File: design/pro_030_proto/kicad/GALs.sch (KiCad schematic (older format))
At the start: 11 parts, among them IC2 ATF22V10C, IC3 ATF22V10C, IC4 ATF22V10C, IC5 ATF22V10C

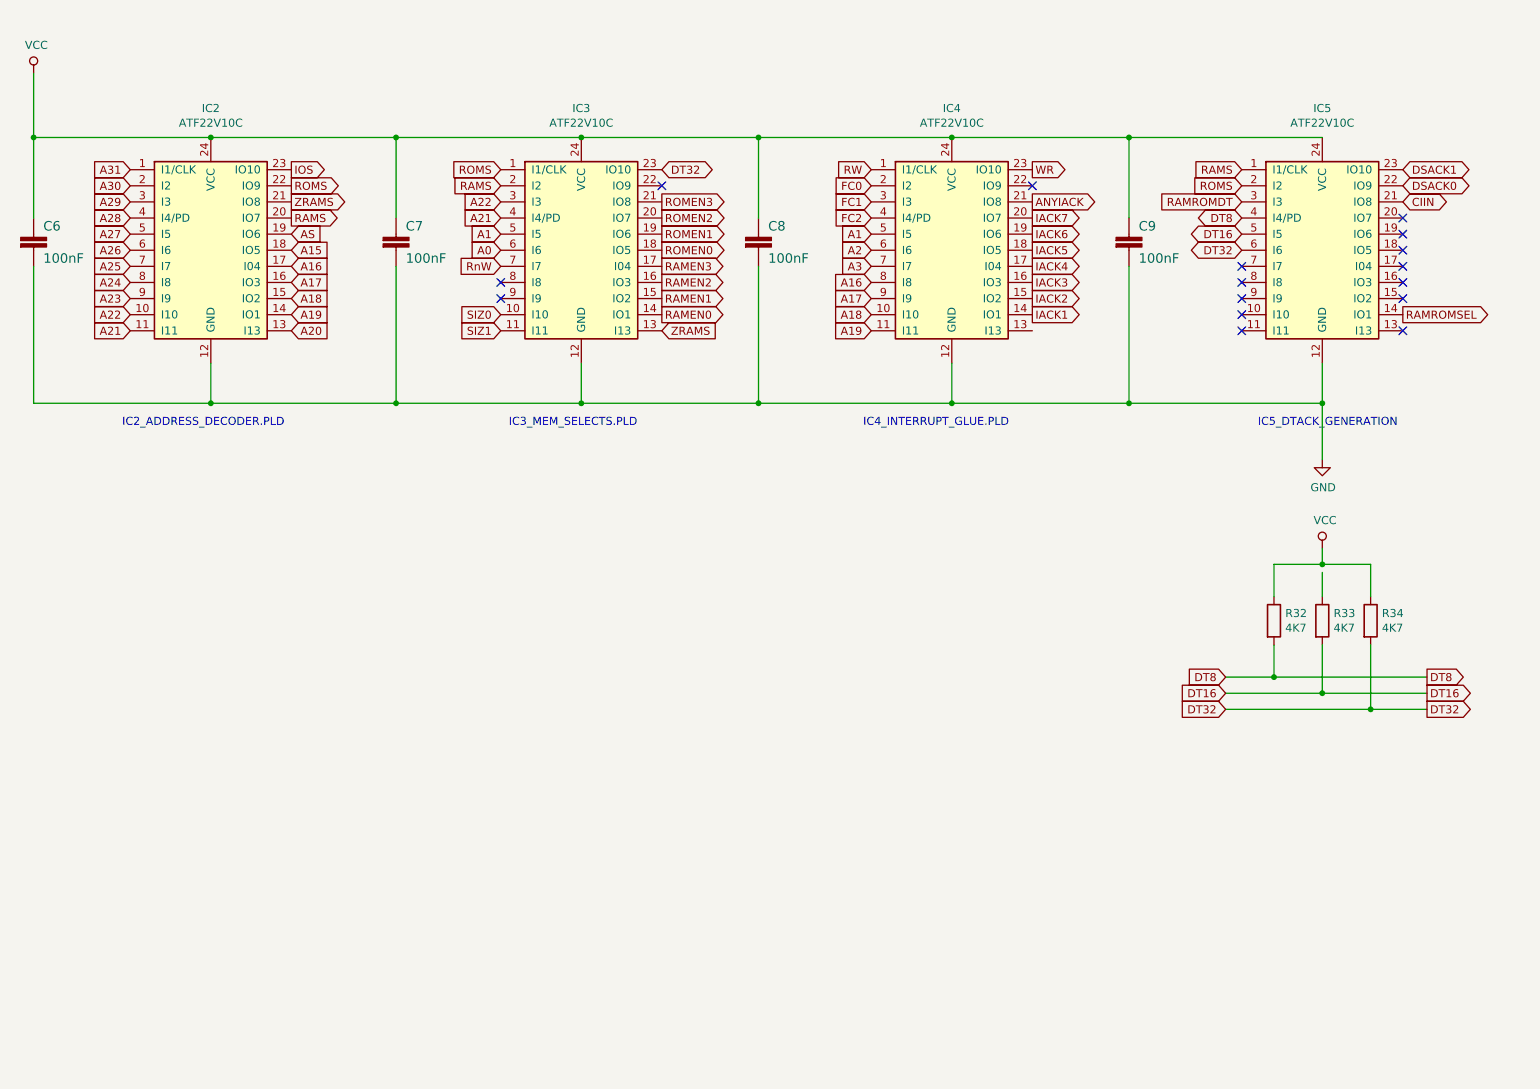
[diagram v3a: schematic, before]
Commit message: Interrupts + Xosera schematic, re-annotate
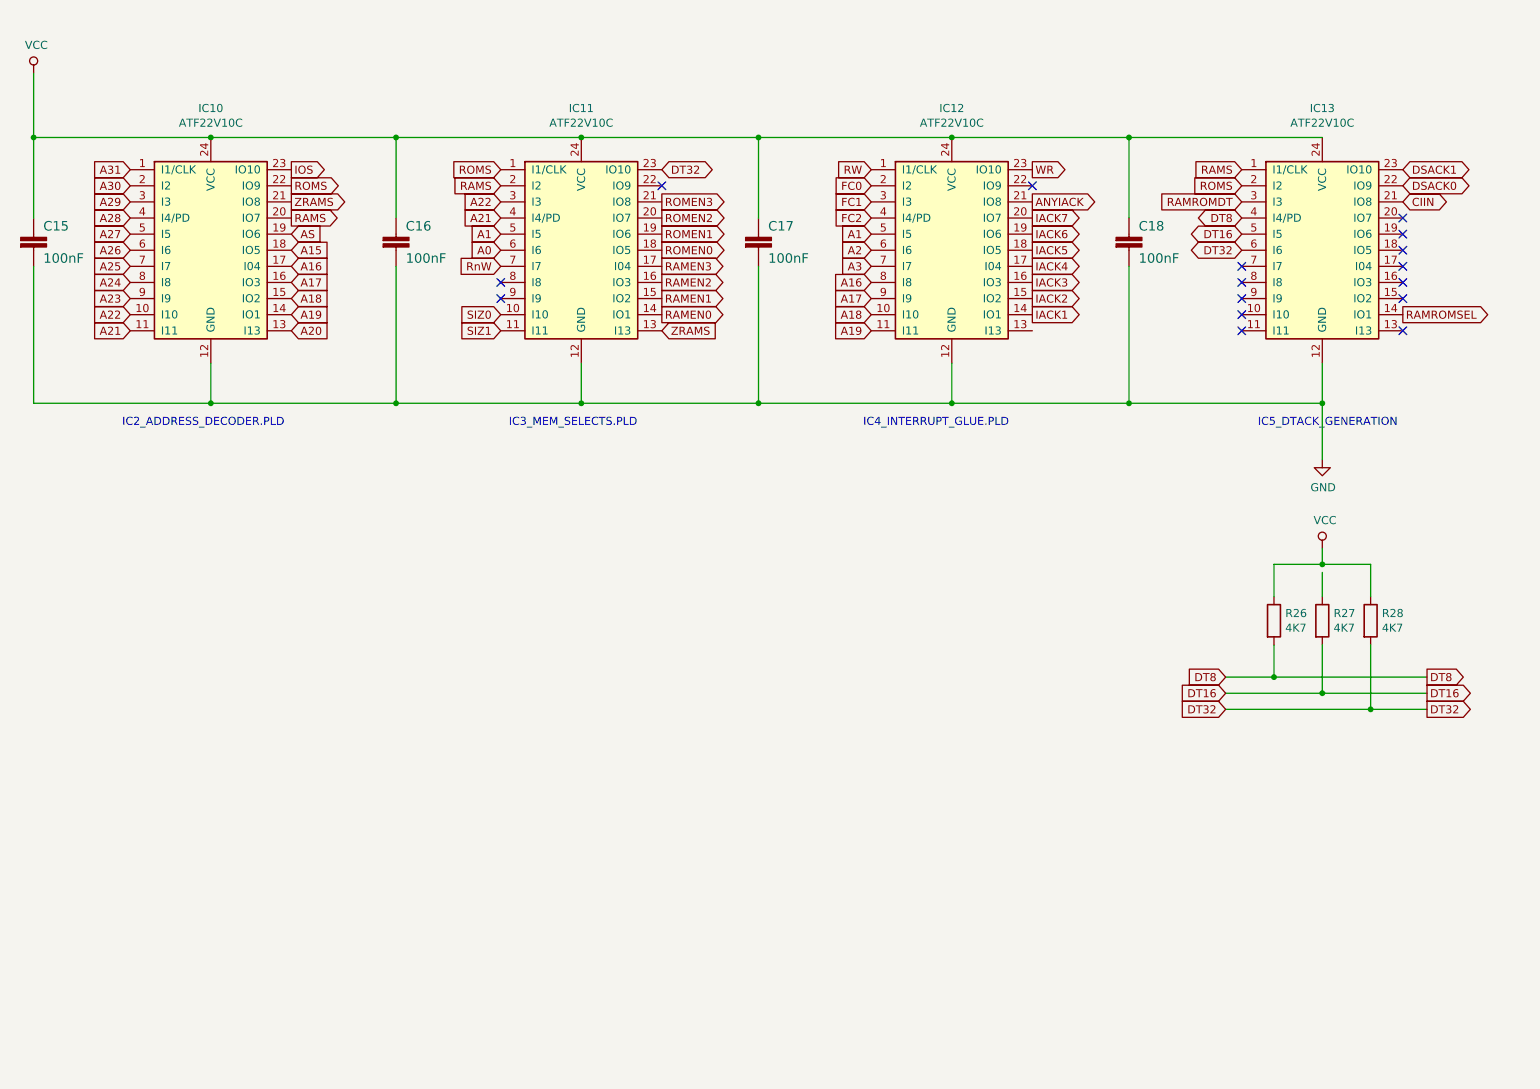
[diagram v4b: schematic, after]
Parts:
- renumbered C6 to C15, C7 to C16, C8 to C17, C9 to C18, IC2 to IC10, IC3 to IC11, IC4 to IC12, IC5 to IC13, R32 to R26, R33 to R27, R34 to R28
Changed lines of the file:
@@
 $Descr A4 11693 8268
 encoding utf-8
-Sheet 7 10
+Sheet 7 13
 Title "rosco_m68k Pro (030) Prototype"
 Date "2021-07-24"
@@
 AR Path="/5E53B810/60FE89A7" Ref="C?"  Part="1"
 AR Path="/5E53B952/60FE89A7" Ref="C?"  Part="1"
-AR Path="/6103896C/60FE89A7" Ref="C7"  Part="1"
-F 0 "C7" H 3610 2165 59  0000 L BNN
+AR Path="/6103896C/60FE89A7" Ref="C16"  Part="1"
+F 0 "C16" H 3610 2165 59  0000 L BNN
 F 1 "100nF" H 3610 1965 59  0000 L BNN
 F 2 "Capacitor_THT:C_Rect_L4.0mm_W2.5mm_P2.50mm" H 3550 2150 50  0001 C CNN
@@
 AR Path="/5E53B810/60F35442" Ref="C?"  Part="1"
 AR Path="/5E53B952/60F35442" Ref="C?"  Part="1"
-AR Path="/6103896C/60F35442" Ref="C8"  Part="1"
-F 0 "C8" H 5860 2165 59  0000 L BNN
+AR Path="/6103896C/60F35442" Ref="C17"  Part="1"
+F 0 "C17" H 5860 2165 59  0000 L BNN
 F 1 "100nF" H 5860 1965 59  0000 L BNN
 F 2 "Capacitor_THT:C_Rect_L4.0mm_W2.5mm_P2.50mm" H 5800 2150 50  0001 C CNN
@@
 AR Path="/5E53B810/60F343B0" Ref="C?"  Part="1"
 AR Path="/5E53B952/60F343B0" Ref="C?"  Part="1"
-AR Path="/6103896C/60F343B0" Ref="C6"  Part="1"
-F 0 "C6" H 1360 2165 59  0000 L BNN
+AR Path="/6103896C/60F343B0" Ref="C15"  Part="1"
+F 0 "C15" H 1360 2165 59  0000 L BNN
 F 1 "100nF" H 1360 1965 59  0000 L BNN
 F 2 "Capacitor_THT:C_Rect_L4.0mm_W2.5mm_P2.50mm" H 1300 2150 50  0001 C CNN
@@
 	4700 2950 4700 3200
 $Comp
-L power:GND #PWR0124
+L power:GND #PWR031
 U 1 1 60F311F4
 P 9300 3550
-F 0 "#PWR0124" H 9300 3300 50  0001 C CNN
+F 0 "#PWR031" H 9300 3300 50  0001 C CNN
 F 1 "GND" H 9305 3377 50  0000 C CNN
 F 2 "" H 9300 3550 50  0001 C CNN
@@
 $EndComp
 $Comp
-L power:VCC #PWR0125
+L power:VCC #PWR030
 U 1 1 60F30787
 P 1300 1150
-F 0 "#PWR0125" H 1300 1000 50  0001 C CNN
+F 0 "#PWR030" H 1300 1000 50  0001 C CNN
 F 1 "VCC" H 1317 1323 50  0000 C CNN
 F 2 "" H 1300 1150 50  0001 C CNN
@@
 ROMS
 $Comp
-L rosco_m68k:GAL22V10 IC3
+L rosco_m68k:GAL22V10 IC11
 U 1 1 60F2CECC
 P 4700 2250
-F 0 "IC3" H 4700 3131 50  0000 C CNN
+F 0 "IC11" H 4700 3131 50  0000 C CNN
 F 1 "ATF22V10C" H 4700 3040 50  0000 C CNN
 F 2 "Package_DIP:DIP-24_W7.62mm_Socket_LongPads" H 4700 2250 50  0001 C CNN
@@
 A31
 $Comp
-L rosco_m68k:GAL22V10 IC2
+L rosco_m68k:GAL22V10 IC10
 U 1 1 60F1E34A
 P 2400 2250
-F 0 "IC2" H 2400 3131 50  0000 C CNN
+F 0 "IC10" H 2400 3131 50  0000 C CNN
 F 1 "ATF22V10C" H 2400 3040 50  0000 C CNN
 F 2 "Package_DIP:DIP-24_W7.62mm_Socket_LongPads" H 2400 2250 50  0001 C CNN
@@
 	7000 3200 7000 2950
 $Comp
-L rosco_m68k:GAL22V10 IC4
+L rosco_m68k:GAL22V10 IC12
 U 1 1 60FE4F51
 P 7000 2250
-F 0 "IC4" H 7000 3131 50  0000 C CNN
+F 0 "IC12" H 7000 3131 50  0000 C CNN
 F 1 "ATF22V10C" H 7000 3040 50  0000 C CNN
 F 2 "Package_DIP:DIP-24_W7.62mm_Socket_LongPads" H 7000 2250 50  0001 C CNN
@@
 AR Path="/5E53B810/610AB2E1" Ref="C?"  Part="1"
 AR Path="/5E53B952/610AB2E1" Ref="C?"  Part="1"
-AR Path="/6103896C/610AB2E1" Ref="C9"  Part="1"
-F 0 "C9" H 8160 2165 59  0000 L BNN
+AR Path="/6103896C/610AB2E1" Ref="C18"  Part="1"
+F 0 "C18" H 8160 2165 59  0000 L BNN
 F 1 "100nF" H 8160 1965 59  0000 L BNN
 F 2 "Capacitor_THT:C_Rect_L4.0mm_W2.5mm_P2.50mm" H 8100 2150 50  0001 C CNN
@@
 NoConn ~ 7500 1850
 $Comp
-L rosco_m68k:GAL22V10 IC5
+L rosco_m68k:GAL22V10 IC13
 U 1 1 610AB2F4
 P 9300 2250
-F 0 "IC5" H 9300 3131 50  0000 C CNN
+F 0 "IC13" H 9300 3131 50  0000 C CNN
 F 1 "ATF22V10C" H 9300 3040 50  0000 C CNN
 F 2 "Package_DIP:DIP-24_W7.62mm_Socket_LongPads" H 9300 2250 50  0001 C CNN
@@
 DT32
 $Comp
-L Device:R R32
+L Device:R R26
 U 1 1 60FCD0F0
 P 9000 4550
-F 0 "R32" H 9070 4596 50  0000 L CNN
+F 0 "R26" H 9070 4596 50  0000 L CNN
 F 1 "4K7" H 9070 4505 50  0000 L CNN
 F 2 "rosco_m68k:R-0207_10" V 8930 4550 50  0001 C CNN
@@
 $EndComp
 $Comp
-L Device:R R33
+L Device:R R27
 U 1 1 60FCDD0E
 P 9300 4550
-F 0 "R33" H 9370 4596 50  0000 L CNN
+F 0 "R27" H 9370 4596 50  0000 L CNN
 F 1 "4K7" H 9370 4505 50  0000 L CNN
 F 2 "rosco_m68k:R-0207_10" V 9230 4550 50  0001 C CNN
@@
 $EndComp
 $Comp
-L Device:R R34
+L Device:R R28
 U 1 1 60FCE353
 P 9600 4550
-F 0 "R34" H 9670 4596 50  0000 L CNN
+F 0 "R28" H 9670 4596 50  0000 L CNN
 F 1 "4K7" H 9670 4505 50  0000 L CNN
 F 2 "rosco_m68k:R-0207_10" V 9530 4550 50  0001 C CNN
@@
 $EndComp
 $Comp
-L power:VCC #PWR0110
+L power:VCC #PWR032
 U 1 1 60FCF006
 P 9300 4100
-F 0 "#PWR0110" H 9300 3950 50  0001 C CNN
+F 0 "#PWR032" H 9300 3950 50  0001 C CNN
 F 1 "VCC" H 9317 4273 50  0000 C CNN
 F 2 "" H 9300 4100 50  0001 C CNN

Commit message: Further layout
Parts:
- renumbered C15 to C14, C16 to C15, C17 to C16, C18 to C17, IC11 to IC10, IC12 to IC11, IC13 to IC12, IC10 to IC9, R26 to R24, R27 to R25, R28 to R26
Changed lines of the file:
@@
 AR Path="/5E53B810/60FE89A7" Ref="C?"  Part="1"
 AR Path="/5E53B952/60FE89A7" Ref="C?"  Part="1"
-AR Path="/6103896C/60FE89A7" Ref="C16"  Part="1"
-F 0 "C16" H 3610 2165 59  0000 L BNN
+AR Path="/6103896C/60FE89A7" Ref="C15"  Part="1"
+F 0 "C15" H 3610 2165 59  0000 L BNN
 F 1 "100nF" H 3610 1965 59  0000 L BNN
 F 2 "Capacitor_THT:C_Rect_L4.0mm_W2.5mm_P2.50mm" H 3550 2150 50  0001 C CNN
@@
 AR Path="/5E53B810/60F35442" Ref="C?"  Part="1"
 AR Path="/5E53B952/60F35442" Ref="C?"  Part="1"
-AR Path="/6103896C/60F35442" Ref="C17"  Part="1"
-F 0 "C17" H 5860 2165 59  0000 L BNN
+AR Path="/6103896C/60F35442" Ref="C16"  Part="1"
+F 0 "C16" H 5860 2165 59  0000 L BNN
 F 1 "100nF" H 5860 1965 59  0000 L BNN
 F 2 "Capacitor_THT:C_Rect_L4.0mm_W2.5mm_P2.50mm" H 5800 2150 50  0001 C CNN
@@
 AR Path="/5E53B810/60F343B0" Ref="C?"  Part="1"
 AR Path="/5E53B952/60F343B0" Ref="C?"  Part="1"
-AR Path="/6103896C/60F343B0" Ref="C15"  Part="1"
-F 0 "C15" H 1360 2165 59  0000 L BNN
+AR Path="/6103896C/60F343B0" Ref="C14"  Part="1"
+F 0 "C14" H 1360 2165 59  0000 L BNN
 F 1 "100nF" H 1360 1965 59  0000 L BNN
 F 2 "Capacitor_THT:C_Rect_L4.0mm_W2.5mm_P2.50mm" H 1300 2150 50  0001 C CNN
@@
 	4700 2950 4700 3200
 $Comp
-L power:GND #PWR031
+L power:GND #PWR030
 U 1 1 60F311F4
 P 9300 3550
-F 0 "#PWR031" H 9300 3300 50  0001 C CNN
+F 0 "#PWR030" H 9300 3300 50  0001 C CNN
 F 1 "GND" H 9305 3377 50  0000 C CNN
 F 2 "" H 9300 3550 50  0001 C CNN
@@
 $EndComp
 $Comp
-L power:VCC #PWR030
+L power:VCC #PWR029
 U 1 1 60F30787
 P 1300 1150
-F 0 "#PWR030" H 1300 1000 50  0001 C CNN
+F 0 "#PWR029" H 1300 1000 50  0001 C CNN
 F 1 "VCC" H 1317 1323 50  0000 C CNN
 F 2 "" H 1300 1150 50  0001 C CNN
@@
 ROMS
 $Comp
-L rosco_m68k:GAL22V10 IC11
+L rosco_m68k:GAL22V10 IC10
 U 1 1 60F2CECC
 P 4700 2250
-F 0 "IC11" H 4700 3131 50  0000 C CNN
+F 0 "IC10" H 4700 3131 50  0000 C CNN
 F 1 "ATF22V10C" H 4700 3040 50  0000 C CNN
 F 2 "Package_DIP:DIP-24_W7.62mm_Socket_LongPads" H 4700 2250 50  0001 C CNN
@@
 A31
 $Comp
-L rosco_m68k:GAL22V10 IC10
+L rosco_m68k:GAL22V10 IC9
 U 1 1 60F1E34A
 P 2400 2250
-F 0 "IC10" H 2400 3131 50  0000 C CNN
+F 0 "IC9" H 2400 3131 50  0000 C CNN
 F 1 "ATF22V10C" H 2400 3040 50  0000 C CNN
 F 2 "Package_DIP:DIP-24_W7.62mm_Socket_LongPads" H 2400 2250 50  0001 C CNN
@@
 	7000 3200 7000 2950
 $Comp
-L rosco_m68k:GAL22V10 IC12
+L rosco_m68k:GAL22V10 IC11
 U 1 1 60FE4F51
 P 7000 2250
-F 0 "IC12" H 7000 3131 50  0000 C CNN
+F 0 "IC11" H 7000 3131 50  0000 C CNN
 F 1 "ATF22V10C" H 7000 3040 50  0000 C CNN
 F 2 "Package_DIP:DIP-24_W7.62mm_Socket_LongPads" H 7000 2250 50  0001 C CNN
@@
 AR Path="/5E53B810/610AB2E1" Ref="C?"  Part="1"
 AR Path="/5E53B952/610AB2E1" Ref="C?"  Part="1"
-AR Path="/6103896C/610AB2E1" Ref="C18"  Part="1"
-F 0 "C18" H 8160 2165 59  0000 L BNN
+AR Path="/6103896C/610AB2E1" Ref="C17"  Part="1"
+F 0 "C17" H 8160 2165 59  0000 L BNN
 F 1 "100nF" H 8160 1965 59  0000 L BNN
 F 2 "Capacitor_THT:C_Rect_L4.0mm_W2.5mm_P2.50mm" H 8100 2150 50  0001 C CNN
@@
 NoConn ~ 7500 1850
 $Comp
-L rosco_m68k:GAL22V10 IC13
+L rosco_m68k:GAL22V10 IC12
 U 1 1 610AB2F4
 P 9300 2250
-F 0 "IC13" H 9300 3131 50  0000 C CNN
+F 0 "IC12" H 9300 3131 50  0000 C CNN
 F 1 "ATF22V10C" H 9300 3040 50  0000 C CNN
 F 2 "Package_DIP:DIP-24_W7.62mm_Socket_LongPads" H 9300 2250 50  0001 C CNN
@@
 DT32
 $Comp
-L Device:R R26
+L Device:R R24
 U 1 1 60FCD0F0
 P 9000 4550
-F 0 "R26" H 9070 4596 50  0000 L CNN
+F 0 "R24" H 9070 4596 50  0000 L CNN
 F 1 "4K7" H 9070 4505 50  0000 L CNN
 F 2 "rosco_m68k:R-0207_10" V 8930 4550 50  0001 C CNN
@@
 $EndComp
 $Comp
-L Device:R R27
+L Device:R R25
 U 1 1 60FCDD0E
 P 9300 4550
-F 0 "R27" H 9370 4596 50  0000 L CNN
+F 0 "R25" H 9370 4596 50  0000 L CNN
 F 1 "4K7" H 9370 4505 50  0000 L CNN
 F 2 "rosco_m68k:R-0207_10" V 9230 4550 50  0001 C CNN
@@
 $EndComp
 $Comp
-L Device:R R28
+L Device:R R26
 U 1 1 60FCE353
 P 9600 4550
-F 0 "R28" H 9670 4596 50  0000 L CNN
+F 0 "R26" H 9670 4596 50  0000 L CNN
 F 1 "4K7" H 9670 4505 50  0000 L CNN
 F 2 "rosco_m68k:R-0207_10" V 9530 4550 50  0001 C CNN
@@
 $EndComp
 $Comp
-L power:VCC #PWR032
+L power:VCC #PWR031
 U 1 1 60FCF006
 P 9300 4100
-F 0 "#PWR032" H 9300 3950 50  0001 C CNN
+F 0 "#PWR031" H 9300 3950 50  0001 C CNN
 F 1 "VCC" H 9317 4273 50  0000 C CNN
 F 2 "" H 9300 4100 50  0001 C CNN
